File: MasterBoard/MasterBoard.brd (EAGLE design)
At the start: 91.3 x 85 mm, 0 parts

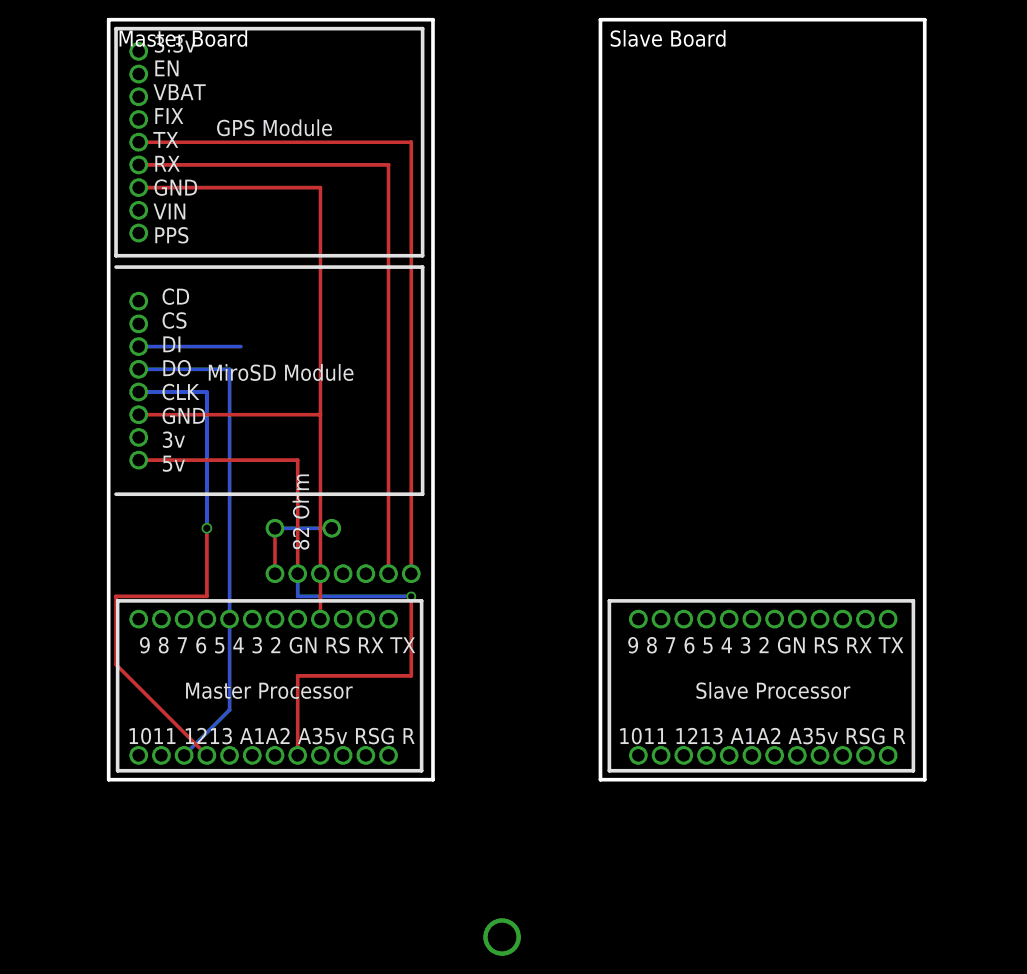
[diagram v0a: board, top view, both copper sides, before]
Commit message: Comoonents Wiring
Wired up Components of master and slave
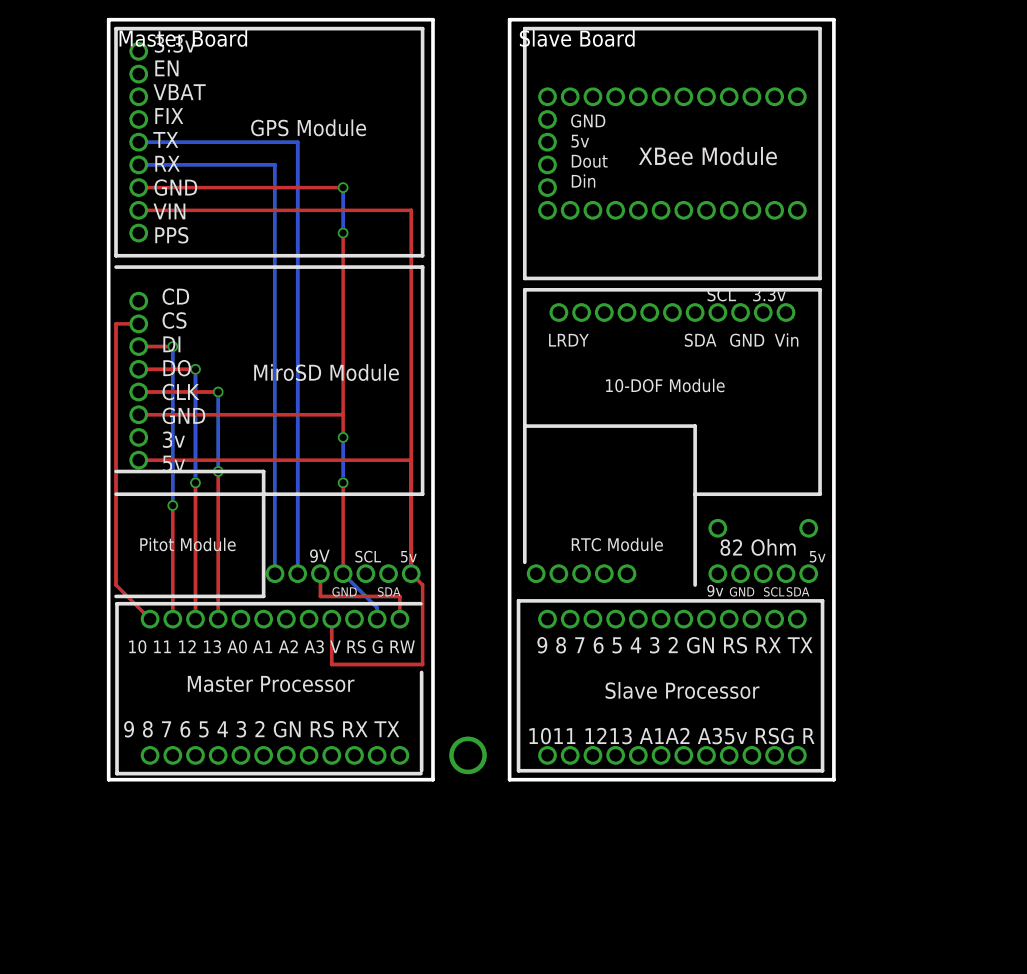
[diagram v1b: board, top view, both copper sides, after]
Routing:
- net S$62: track 0.00 -> 95.6 mm, vias 1 -> 8
- net S$58: track 88.9 -> 0.00 mm, vias 4 -> 0
- net S$21: track 76.2 -> 140.2 mm
- net S$54: track 55.4 -> 0.00 mm, vias 2 -> 0
- net S$68: track 0.00 -> 37.1 mm, vias 1 -> 2
- net S$10: track 0.00 -> 34.3 mm, vias 1 -> 4
- net S$4: track 62.6 -> 34.3 mm, vias 3 -> 4
- net S$67: track 11.4 -> 34.3 mm, vias 1 -> 4
- net S$71: track 0.00 -> 14.0 mm, vias 0 -> 2
- net S$64: track 78.7 -> 66.0 mm
- net S$63: track 73.7 -> 61.0 mm
- net S$8: track 11.4 -> 0.00 mm, vias 3 -> 1
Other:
- board size 91.3 x 85 mm -> 81.1 x 85 mm
- board text added: "10 11 12 13 A0 A1 A2 A3 V RS G RW"
- board text added: "10-DOF Module"
- board text added: "3.3v"
- board text added: "5v"
- board text added: "9V"
- board text added: "9v"
- board text added: "GND"
- board text added: "GND 5v Dout Din"
- board text added: "LRDY"
- board text added: "Pitot Module"
- board text added: "RTC Module"
- board text added: "SCL"
- board text added: "SDA"
- board text added: "THE GLORY OF RYERSON"
- board text added: "Vin"
- board text added: "XBee Module"

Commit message: Just did some slave wiring
Just did some slave wiring
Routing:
- net S$82: track 0.00 -> 227.1 mm, vias 0 -> 10
- net S$46: track 0.00 -> 159.4 mm, vias 1 -> 6
- net S$1: track 0.00 -> 65.9 mm, vias 0 -> 4
- net S$58: track 0.00 -> 35.7 mm, vias 0 -> 3
- net S$12: track 0.00 -> 35.1 mm, vias 0 -> 2
- net S$9: track 0.00 -> 28.7 mm, vias 0 -> 1
- net S$44: track 0.00 -> 20.3 mm, vias 1 -> 3
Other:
- board text added: "5V"
- board text added: "R_Button"
- board text added: "SQW"
- board text removed: "1011 1213 A1A2 A35v RSG R"
